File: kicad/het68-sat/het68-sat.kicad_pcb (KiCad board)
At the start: 2 copper layers, 28 x 52 mm, 10 parts, among them J1 RJ45, U1 AP2112K-1.8

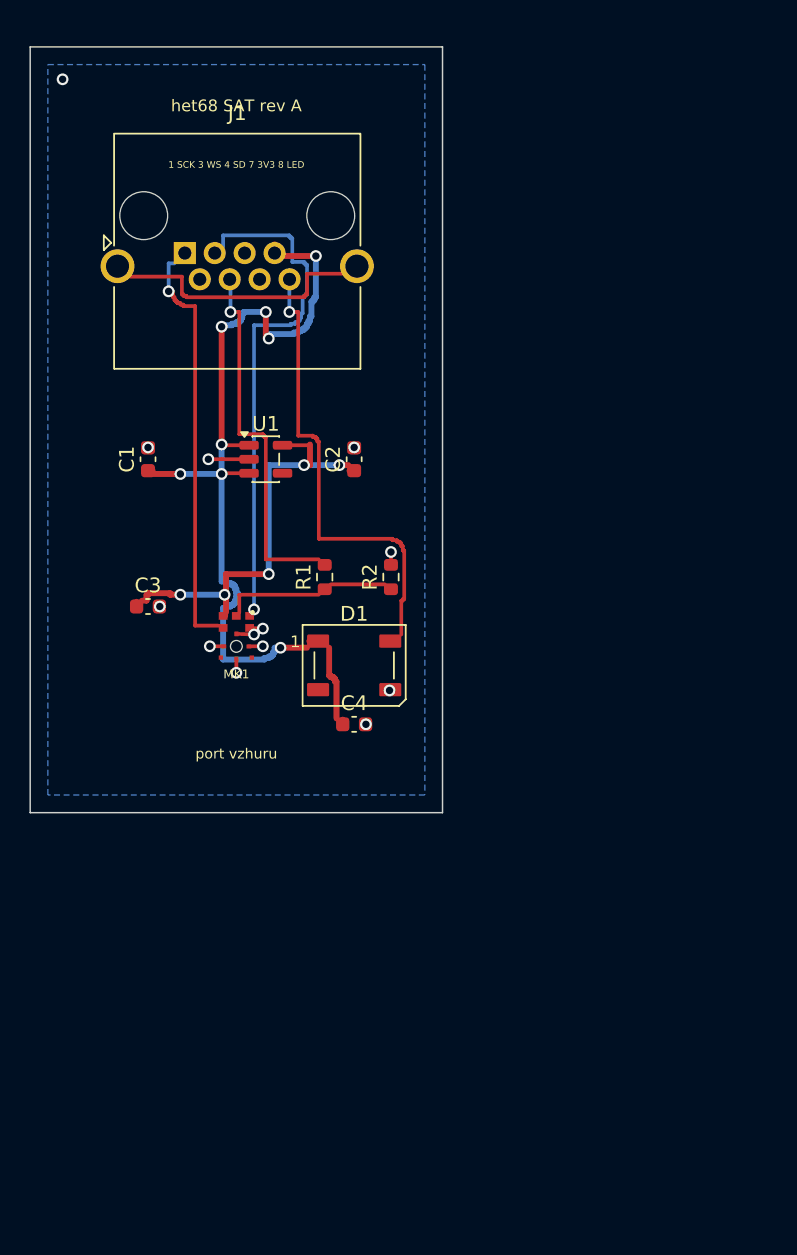
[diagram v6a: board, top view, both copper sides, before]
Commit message: Freeze v4 as a native RP2350B 6-layer core with a swappable CT-secondary power board.
MeshCore stays on Heltec V3 via J_MESH so the node remains in the mesh while DSP sleeps; satellites move to LVDS, and mains voltage never lands on copper.

Co-authored-by: Cursor <cursoragent@cursor.com>
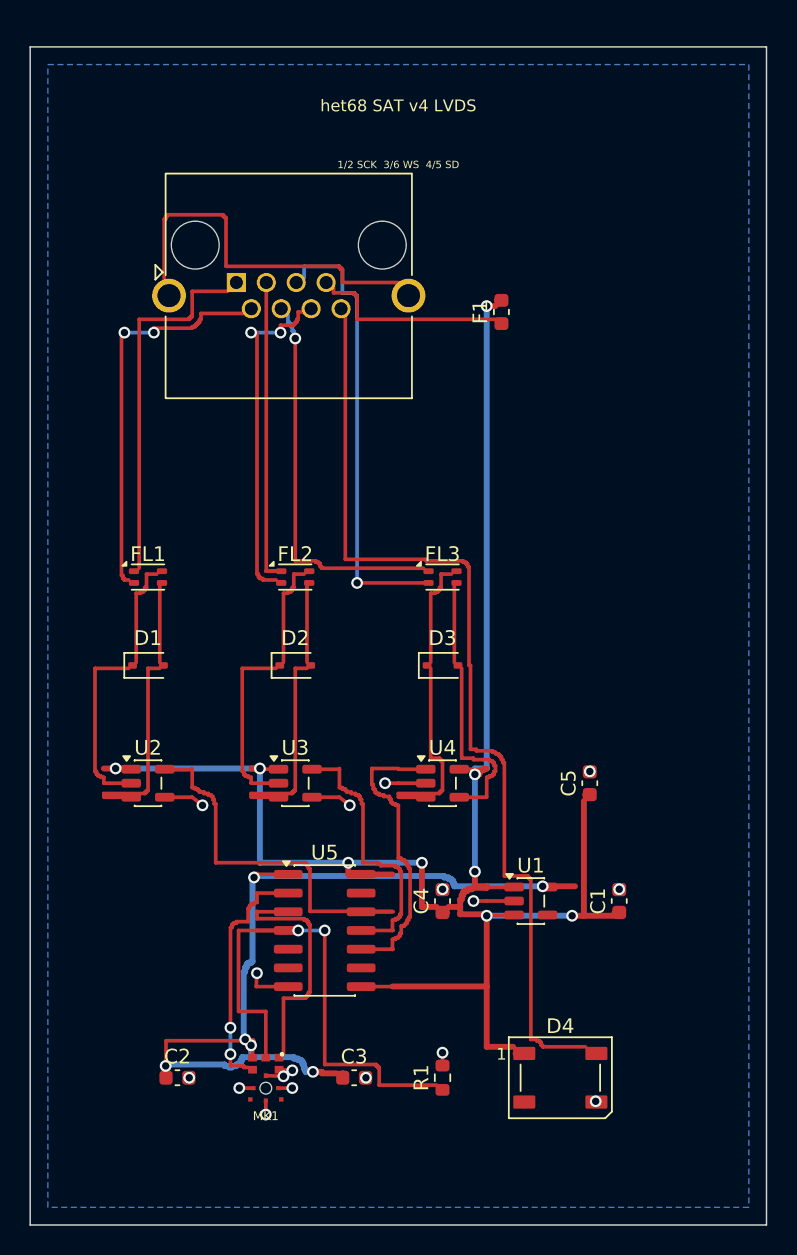
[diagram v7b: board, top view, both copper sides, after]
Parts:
- removed R2: 100k, Resistor_SMD:R_0603_1608Metric
- added C5: 100n, Capacitor_SMD:C_0603_1608Metric, F.Cu at (38.0, 50.0)
- added D2: PESD5V0X1BT, Diode_SMD:D_SOD-323, F.Cu at (18.0, 42.0)
- added D3: PESD5V0X1BT, Diode_SMD:D_SOD-323, F.Cu at (28.0, 42.0)
- added D4: SK6812, LED_SMD:LED_WS2812B_PLCC4_5.0x5.0mm_P3.2mm, F.Cu at (36.0, 70.0)
- added F1: 0.25A, Fuse:Fuse_0603_1608Metric, F.Cu at (32.0, 18.0)
- added FL1: CMC, Inductor_SMD:L_CommonModeChoke_Coilank_ACM2012, F.Cu at (8.00, 36.0)
- added FL2: CMC, Inductor_SMD:L_CommonModeChoke_Coilank_ACM2012, F.Cu at (18.0, 36.0)
- added FL3: CMC, Inductor_SMD:L_CommonModeChoke_Coilank_ACM2012, F.Cu at (28.0, 36.0)
- added U2: SN65LVDS2, Package_TO_SOT_SMD:SOT-23-5, F.Cu at (8.00, 50.0)
- added U3: SN65LVDS2, Package_TO_SOT_SMD:SOT-23-5, F.Cu at (18.0, 50.0)
- added U4: SN65LVDS1, Package_TO_SOT_SMD:SOT-23-5, F.Cu at (28.0, 50.0)
- added U5: TXS0104E, Package_SO:SOIC-14_3.9x8.7mm_P1.27mm, F.Cu at (20.0, 60.0)
- D1: value SK6812 -> PESD5V0X1BT; footprint LED_SMD:LED_WS2812B_PLCC4_5.0x5.0mm_P3.2mm -> Diode_SMD:D_SOD-323
- J1: footprint Connector_RJ:RJ45_Amphenol_RJHSE5380 -> het68:RJ45_RJHSE5380_het68
- R1: value 33 -> 100k
- moved C1 43.9 mm to (40.0, 58.0)
- moved C2 43.7 mm to (10.0, 70.0), turned to 0 degrees
- moved U1 35.0 mm to (34.0, 58.0)
- moved C3 34.9 mm to (22.0, 70.0)
- moved R1 34.9 mm to (28.0, 70.0)
- moved MK1 30.1 mm to (16.0, 70.0)
- moved D1 14.0 mm to (8.00, 42.0)
- moved C4 13.4 mm to (28.0, 58.0), turned to 90 degrees
- moved J1 4.03 mm to (14.0, 16.0)
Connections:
- D1 pad 1: +3V3 -> SCK_P
- D1 pad 2: unconnected-(D1-DOUT-Pad2) -> SCK_N
- J1 pad 1: SCK -> SCK_PJ
- J1 pad 2: GND -> SCK_NJ
- J1 pad 3: WS -> WS_PJ
- J1 pad 4: SD_J -> SD_PJ
- J1 pad 5: GND -> SD_NJ
- J1 pad 6: GND -> WS_NJ
- J1 pad 7: +3V3 -> 3V3_F
- R1 pad 2: SD_J -> GND
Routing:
- net +3V3: track 63.7 -> 134.6 mm, vias 8 -> 9
- net +1V8: track 29.0 -> 65.0 mm, vias 5 -> 6
- net LED: track 32.6 -> 67.0 mm, vias 1 -> 0
- net SD_NJ: track 0.00 -> 31.1 mm, vias 0 -> 1
- net SCK_NJ: track 0.00 -> 27.6 mm, vias 0 -> 2
- net SCK_3V3: track 0.00 -> 27.3 mm
- net SD_PJ: track 0.00 -> 27.1 mm, vias 0 -> 1
- net SD: track 11.1 -> 36.9 mm, vias 0 -> 2
- net SCK_PJ: track 0.00 -> 25.5 mm
- net SD_J: track 25.2 -> 0.00 mm, vias 1 -> 0
- net WS_NJ: track 0.00 -> 24.1 mm, vias 0 -> 2
- net SD_P: track 0.00 -> 22.1 mm
- net SD_3V3: track 0.00 -> 21.9 mm
- net WS_PJ: track 0.00 -> 21.6 mm
- net SCK_P: track 0.00 -> 20.3 mm
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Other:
- board size 28 x 52 mm -> 50 x 80 mm
- board text added: "1/2 SCK 3/6 WS 4/5 SD"
- board text added: "het68 SAT v4 LVDS"
- board text removed: "1 SCK 3 WS 4 SD 7 3V3 8 LED"
- board text removed: "het68 SAT rev A"
- board text removed: "port vzhuru"

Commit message: Give the satellite the same 6-layer Faraday stack as Core and an 8-LED ring.
Mic data sat→Core already uses SN65LVDS1 into SN65LVDS32; SCK/WS stay LVDS the other way.

Co-authored-by: Cursor <cursoragent@cursor.com>
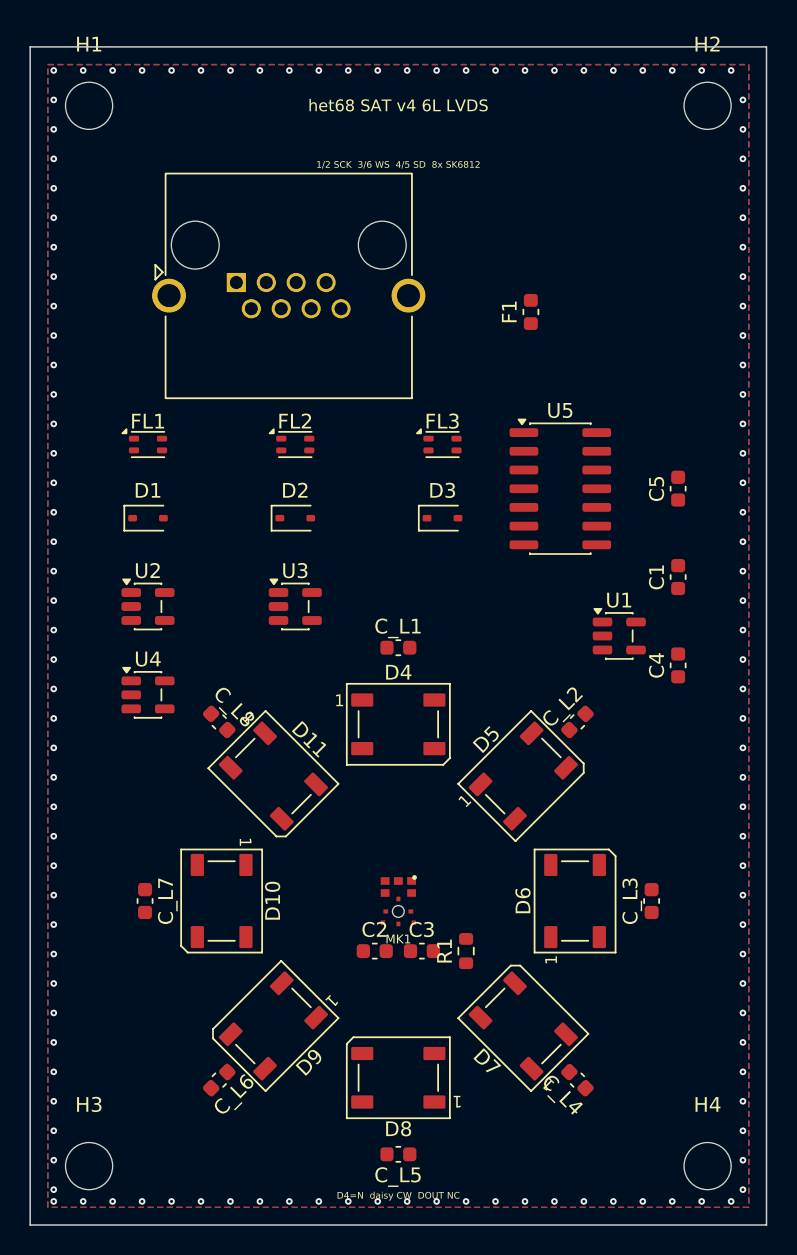
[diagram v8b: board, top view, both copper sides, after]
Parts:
- added C_L1: 100n, Capacitor_SMD:C_0603_1608Metric, F.Cu at (25.0, 40.8)
- added C_L2: 100n, Capacitor_SMD:C_0603_1608Metric, F.Cu at (37.2, 45.8)
- added C_L3: 100n, Capacitor_SMD:C_0603_1608Metric, F.Cu at (42.2, 58.0)
- added C_L4: 100n, Capacitor_SMD:C_0603_1608Metric, F.Cu at (37.2, 70.2)
- added C_L5: 100n, Capacitor_SMD:C_0603_1608Metric, F.Cu at (25.0, 75.2)
- added C_L6: 100n, Capacitor_SMD:C_0603_1608Metric, F.Cu at (12.8, 70.2)
- added C_L7: 100n, Capacitor_SMD:C_0603_1608Metric, F.Cu at (7.80, 58.0)
- added C_L8: 100n, Capacitor_SMD:C_0603_1608Metric, F.Cu at (12.8, 45.8)
- added D10: SK6812, LED_SMD:LED_WS2812B_PLCC4_5.0x5.0mm_P3.2mm, F.Cu at (13.0, 58.0)
- added D11: SK6812, LED_SMD:LED_WS2812B_PLCC4_5.0x5.0mm_P3.2mm, F.Cu at (16.5, 49.5)
- added D5: SK6812, LED_SMD:LED_WS2812B_PLCC4_5.0x5.0mm_P3.2mm, F.Cu at (33.5, 49.5)
- added D6: SK6812, LED_SMD:LED_WS2812B_PLCC4_5.0x5.0mm_P3.2mm, F.Cu at (37.0, 58.0)
- added D7: SK6812, LED_SMD:LED_WS2812B_PLCC4_5.0x5.0mm_P3.2mm, F.Cu at (33.5, 66.5)
- added D8: SK6812, LED_SMD:LED_WS2812B_PLCC4_5.0x5.0mm_P3.2mm, F.Cu at (25.0, 70.0)
- added D9: SK6812, LED_SMD:LED_WS2812B_PLCC4_5.0x5.0mm_P3.2mm, F.Cu at (16.5, 66.5)
- added H1: M3, MountingHole:MountingHole_3.2mm_M3, F.Cu at (4.00, 4.00)
- added H2: M3, MountingHole:MountingHole_3.2mm_M3, F.Cu at (46.0, 4.00)
- added H3: M3, MountingHole:MountingHole_3.2mm_M3, F.Cu at (4.00, 76.0)
- added H4: M3, MountingHole:MountingHole_3.2mm_M3, F.Cu at (46.0, 76.0)
- F1: value 0.25A -> 0.5A
- moved U5 34.0 mm to (36.0, 30.0)
- moved D4 26.4 mm to (25.0, 46.0)
- moved C4 22.6 mm to (44.0, 42.0)
- moved C1 22.4 mm to (44.0, 36.0)
- moved C5 20.9 mm to (44.0, 30.0)
- moved U4 20.9 mm to (8.00, 44.0)
- moved U1 19.0 mm to (40.0, 40.0)
- moved C2 15.9 mm to (23.4, 61.4)
- moved MK1 15.0 mm to (25.0, 58.0)
- moved U2 12.0 mm to (8.00, 38.0)
- moved U3 12.0 mm to (18.0, 38.0)
- moved D1 10.0 mm to (8.00, 32.0)
- moved D2 10.0 mm to (18.0, 32.0)
- moved D3 10.0 mm to (28.0, 32.0)
- moved C3 9.75 mm to (26.6, 61.4)
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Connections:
- D4 pad 2: unconnected-(D4-DOUT-Pad2) -> LED2
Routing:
- net +3V3: track 134.6 -> 0.00 mm, vias 9 -> 0
- net LED: track 67.0 -> 0.00 mm
- net +1V8: track 65.0 -> 0.00 mm, vias 6 -> 0
- net SD: track 36.9 -> 0.00 mm, vias 2 -> 0
- net SD_NJ: track 31.1 -> 0.00 mm, vias 1 -> 0
- net SCK_NJ: track 27.6 -> 0.00 mm, vias 2 -> 0
- net SCK_3V3: track 27.3 -> 0.00 mm
- net SD_PJ: track 27.1 -> 0.00 mm, vias 1 -> 0
- net unconnected-(J1-SHIELD-PadSH): track 27.0 -> 0.00 mm
- net SCK_PJ: track 25.5 -> 0.00 mm
- net WS_NJ: track 24.1 -> 0.00 mm, vias 2 -> 0
- net SD_P: track 22.1 -> 0.00 mm
- net SD_3V3: track 21.9 -> 0.00 mm
- net WS_PJ: track 21.6 -> 0.00 mm
- net SCK_P: track 20.3 -> 0.00 mm
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- added copper zone on In3.Cu, net +1V8
- added copper zone on In3.Cu, net +3V3
- added copper zone on F.Cu, net GND
- added copper zone on In1.Cu, net GND
- added copper zone on In2.Cu, net GND
- added copper zone on In4.Cu, net GND
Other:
- copper layers 2 -> 6
- board text added: "1/2 SCK 3/6 WS 4/5 SD 8x SK6812"
- board text added: "D4=N daisy CW DOUT NC"
- board text added: "het68 SAT v4 6L LVDS"
- board text removed: "1/2 SCK 3/6 WS 4/5 SD"
- board text removed: "het68 SAT v4 LVDS"
